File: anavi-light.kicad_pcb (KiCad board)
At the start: 2 copper layers, 65 x 30 mm, 27 parts, among them Q1 IRF8721PBF-1, Q2 IRF8721PBF-1, Q3 IRF8721PBF-1, U1 CAT24C32WI-GT3

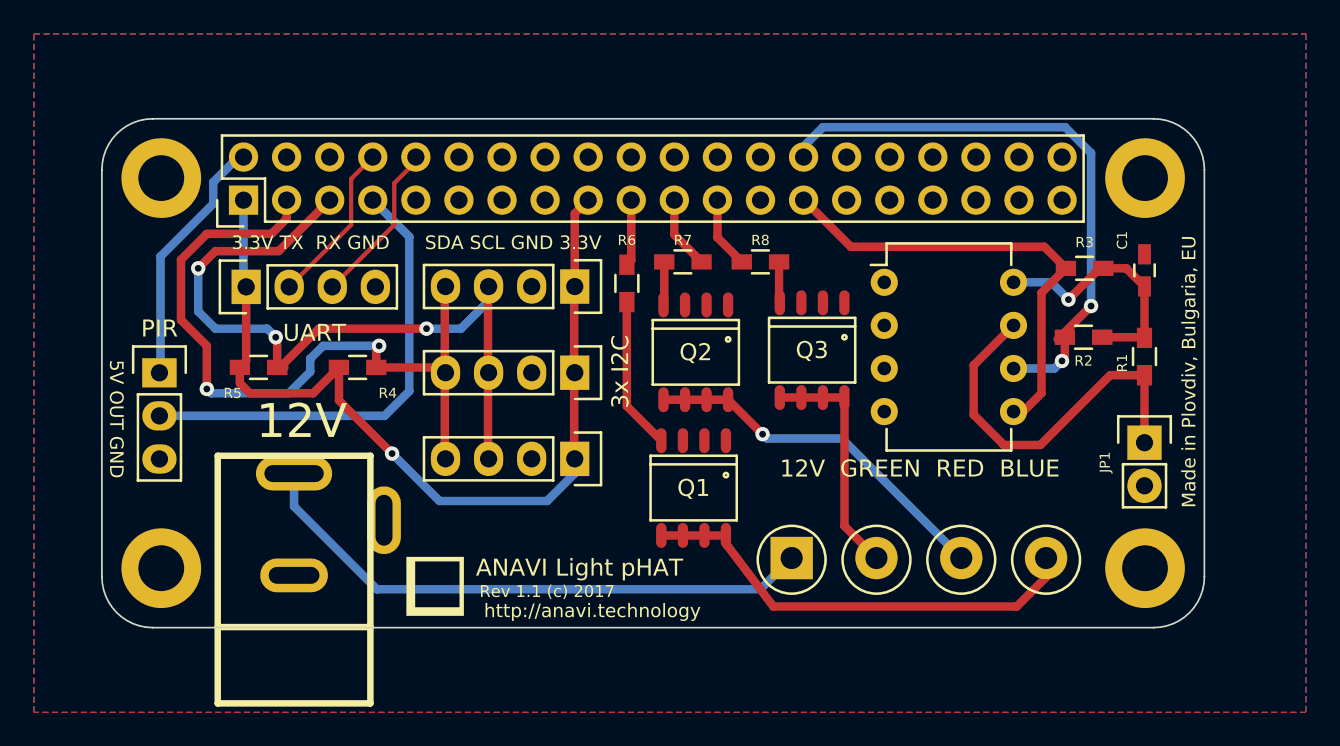
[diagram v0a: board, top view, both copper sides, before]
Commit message: anavi-light: Port to KiCad 6
Port project to KiCad 6.

Signed-off-by: Leon Anavi <leon@anavi.org>
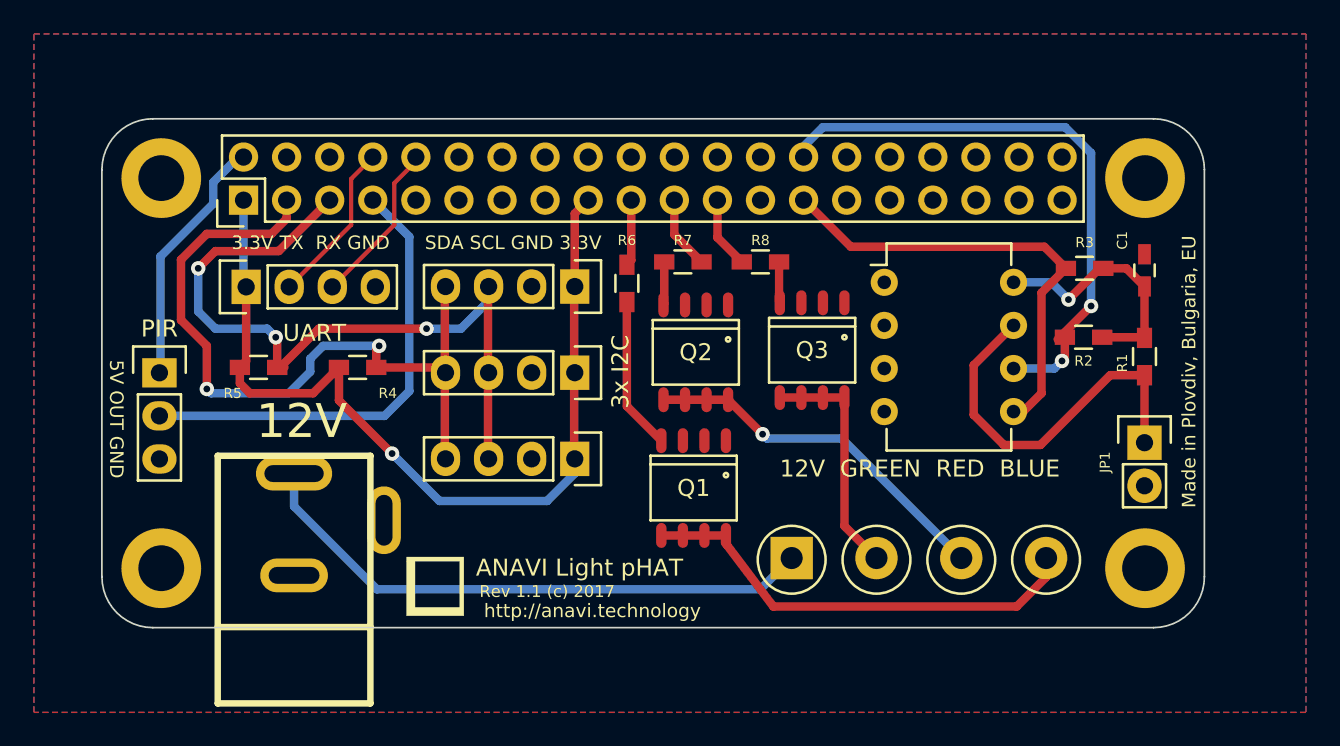
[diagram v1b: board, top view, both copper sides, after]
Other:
- net class Default removed
- net class vcc removed
